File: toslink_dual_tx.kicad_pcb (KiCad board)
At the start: 2 copper layers, 65.8 x 46.9 mm, 20 parts, among them J1 Conn_01x04_Pin, J2 Conn_01x01_Pin, J3 Conn_01x06_Pin, J4 Conn_01x06_Pin, U1 L7805, U2 74HC86, U3 74HC00

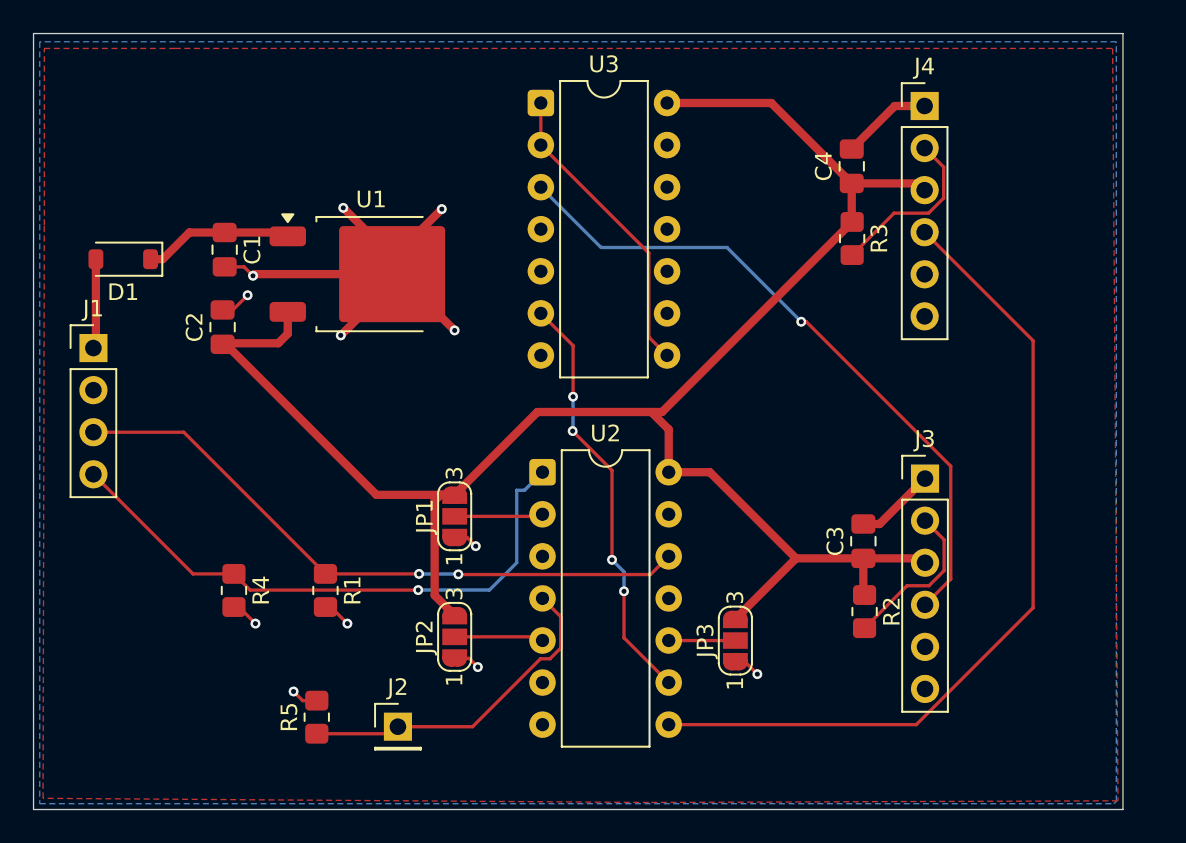
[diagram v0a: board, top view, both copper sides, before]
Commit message: changed from DIL to SO-14 ICs
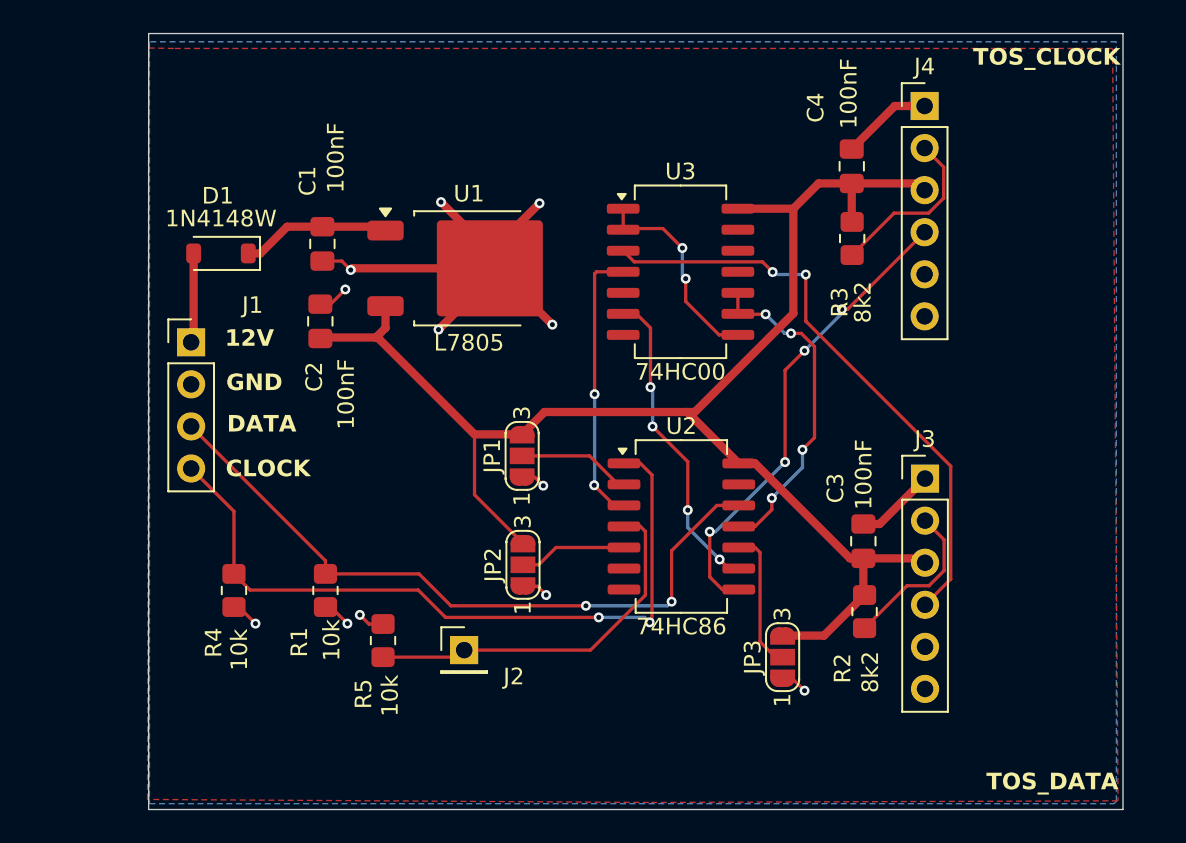
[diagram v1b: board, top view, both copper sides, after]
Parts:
- U2, U3: footprint Package_DIP:DIP-14_W7.62mm -> Package_SO:SO-14_5.3x10.2mm_P1.27mm
- moved U3 13.2 mm to (96.8, 70.7)
- moved U2 9.00 mm to (96.8, 86.1)
- moved J2 6.11 mm to (83.7, 93.5)
- moved R5 6.11 mm to (78.8, 93.0)
- moved JP2 5.99 mm to (87.3, 88.4)
- moved C2 5.91 mm to (75.0, 73.7)
- moved U1 5.91 mm to (84.0, 70.5)
- moved C1 5.91 mm to (75.2, 69.0)
- moved D1 5.91 mm to (69.0, 69.6)
- moved J1 5.91 mm to (67.2, 74.9)
- moved JP1 5.47 mm to (87.2, 81.8)
- moved JP3 3.02 mm to (103.0, 94.0)
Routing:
- net Net-(J4-Pin_4): track 50.3 -> 28.7 mm, vias 0 -> 4
- net 5V: track 112.2 -> 91.2 mm
- net Net-(U2-Pad11): track 0.00 -> 20.0 mm, vias 0 -> 4
- net Net-(U2-Pad3): track 0.00 -> 16.9 mm, vias 0 -> 2
- net CLOCK: track 35.5 -> 44.7 mm, vias 1 -> 2
- net Net-(U2-Pad9): track 25.5 -> 19.1 mm
- net Net-(U3-Pad1): track 18.4 -> 12.7 mm, vias 0 -> 2
- net Net-(J3-Pin_4): track 40.7 -> 35.8 mm, vias 1 -> 2
- net Net-(JP3-C): track 4.03 -> 8.55 mm
- net DATA: track 38.8 -> 42.3 mm
- net Net-(J2-Pin_1): track 20.3 -> 22.7 mm
- net Net-(JP1-C): track 5.36 -> 6.86 mm
- net Net-(JP2-C): track 5.40 -> 6.53 mm
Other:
- board size 65.8 x 46.9 mm -> 58.8 x 46.9 mm
- board text added: "12V"
- board text added: "CLOCK"
- board text added: "DATA"
- board text added: "GND"
- board text added: "TOS_CLOCK"
- board text added: "TOS_DATA"

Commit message: added TOTX173 symbols and footprints
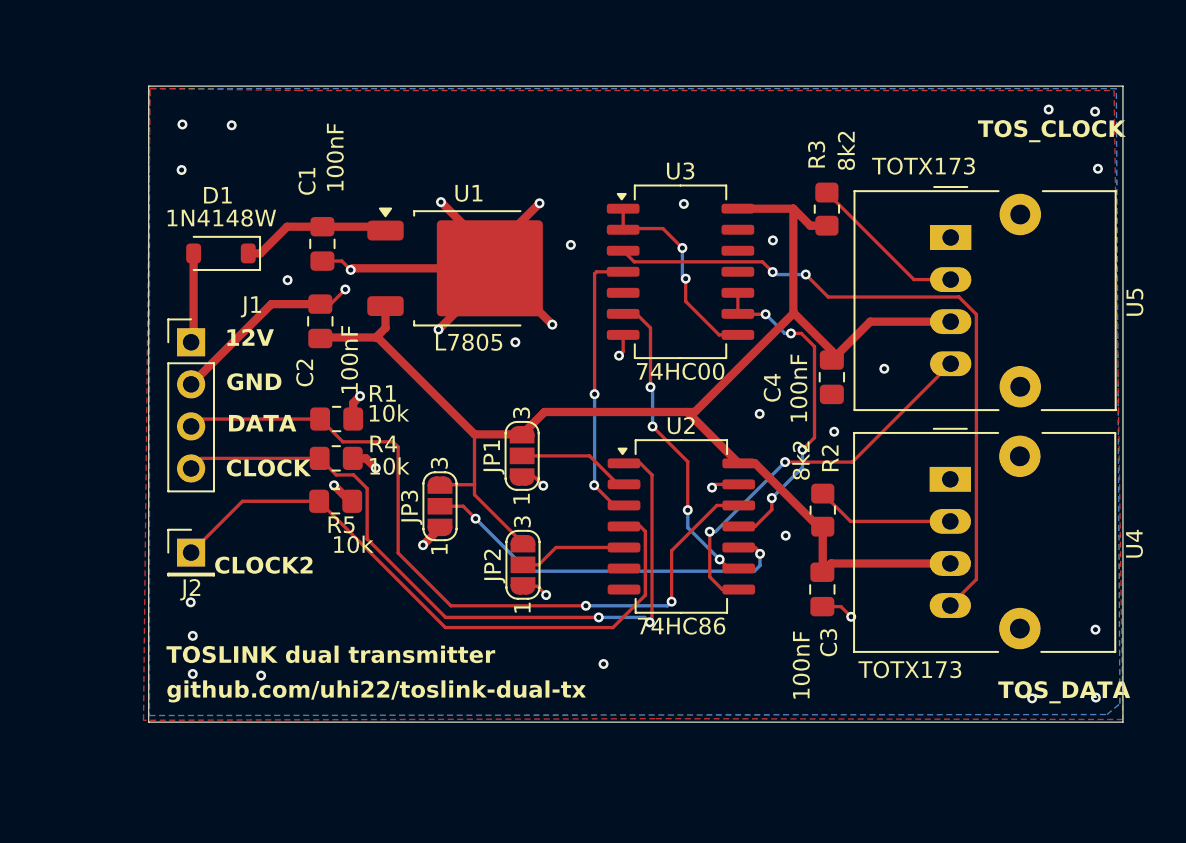
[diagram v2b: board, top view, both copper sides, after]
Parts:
- removed J3, J4: Conn_01x06_Pin, Connector_PinHeader_2.54mm:PinHeader_1x06_P2.54mm_Vertical
- added U4: TOTX173, OptoDevice:Toshiba_TOTX170_TOTX173_TOTX193_TOTX194, F.Cu at (113.1, 83.2)
- added U5: TOTX173, OptoDevice:Toshiba_TOTX170_TOTX173_TOTX193_TOTX194, F.Cu at (113.1, 68.6)
- moved JP3 22.6 mm to (82.3, 84.8)
- moved J2 17.5 mm to (67.2, 87.6)
- moved C4 12.8 mm to (105.9, 77.0), turned to -90 degrees
- moved R1 10.4 mm to (76.0, 79.6), turned to 0 degrees
- moved R4 10.1 mm to (76.0, 82.0), turned to 0 degrees
- moved R5 8.88 mm to (76.0, 84.5), turned to 0 degrees
- moved R2 6.63 mm to (105.4, 85.1), turned to 90 degrees
- moved C3 3.82 mm to (105.3, 89.9), turned to -90 degrees
- moved R3 2.34 mm to (105.6, 66.9), turned to 90 degrees
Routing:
- net Net-(J2-Pin_1): track 22.7 -> 37.9 mm
- net Net-(JP3-C): track 8.55 -> 23.3 mm, vias 0 -> 2
- net Net-(U4-INPUT): track 35.8 -> 41.1 mm
- net Net-(U5-INPUT): track 28.7 -> 23.5 mm, vias 4 -> 2
- net DATA: track 42.3 -> 46.0 mm
- net GND: track 53.3 -> 56.9 mm, vias 12 -> 38
- net Net-(U4-R): track 9.73 -> 8.40 mm
- net 5V: track 91.2 -> 92.1 mm
- net Net-(U5-R): track 10.4 -> 9.65 mm
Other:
- board size 58.8 x 46.9 mm -> 58.8 x 38.4 mm
- board text added: "CLOCK2"
- board text added: "TOSLINK dual transmitter"
- board text added: "github.com/uhi22/toslink-dual-tx"
